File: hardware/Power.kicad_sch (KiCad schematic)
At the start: 36 parts, among them IC1 TPS54202HDDCR, Q1 SI2347DS-T1-GE3, T10 TP_+5V, T11 TP_+5V, T3 TP_VCC, T8 TP_VCC, T9 TP_+3V3, U2 LM1117-3.3

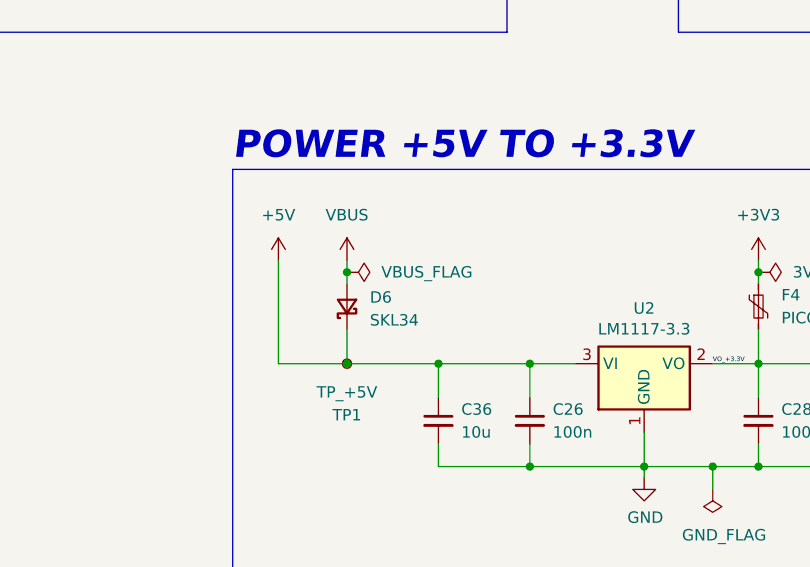
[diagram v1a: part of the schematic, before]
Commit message: power section and isocan layout
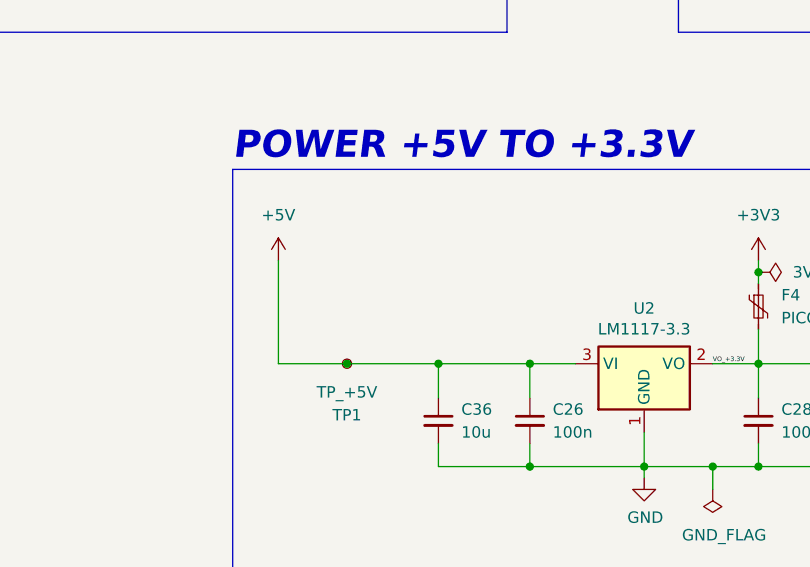
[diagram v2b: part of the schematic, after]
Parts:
- removed D6: SKL34, Diode_SMD:D_SOD-123F, symbol Device:D_Schottky_Small
